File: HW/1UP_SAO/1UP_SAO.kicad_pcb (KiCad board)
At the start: 2 copper layers, 48 x 48 mm, 17 parts, among them X1 Badgelife_sao_connector_v169b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

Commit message: done?
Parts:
- moved R1 0.10 mm to (85.9, 101.5)
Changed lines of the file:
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@@
   )
   (module Resistor_SMD:R_0805_2012Metric_Pad1.15x1.40mm_HandSolder (layer B.Cu)
-    (at 85.8 101.5 180)
+    (at 85.9 101.5 180)
     (descr "Resistor SMD 0805 (2012 Metric), square (rectangular) end terminal, IPC_7351 nominal with elongated pad for handsoldering. (Body size source: https://docs.google.com/spreadsheets/d/1BsfQQcO9C6DZCsRaXUlFlo91Tg2WpOkGARC1WS5S8t0/edit?usp=sharing), generated with kicad-footprint-generator")
     (tags "resistor handsolder")
@@
   (segment (start 111.19559 102.27941) (end 111.975 101.5) (width 0.254) (layer B.Cu) (net 8))
   (segment (start 107.47059 102.27941) (end 111.19559 102.27941) (width 0.254) (layer B.Cu) (net 8))
-  (segment (start 92.75 102.5) (end 91.125 102.5) (width 0.254) (layer B.Cu) (net 8))
-  (segment (start 93.25 103) (end 92.75 102.5) (width 0.254) (layer B.Cu) (net 8))
+  (segment (start 111.975 101.5) (end 113.075 101.5) (width 0.254) (layer B.Cu) (net 8))
+  (segment (start 92.6 102.6) (end 91.225 102.6) (width 0.254) (layer B.Cu) (net 8))
+  (segment (start 93.25 103.25) (end 92.6 102.6) (width 0.254) (layer B.Cu) (net 8))
   (segment (start 97.52 107.75) (end 96.656401 106.886401) (width 0.254) (layer B.Cu) (net 8))
+  (segment (start 90.225 101.6) (end 87.2 101.6) (width 0.254) (layer B.Cu) (net 8))
   (segment (start 96.656401 106.886401) (end 94.136401 106.886401) (width 0.254) (layer B.Cu) (net 8))
-  (segment (start 91.125 102.5) (end 90.225 101.6) (width 0.254) (layer B.Cu) (net 8))
+  (segment (start 91.225 102.6) (end 90.225 101.6) (width 0.254) (layer B.Cu) (net 8))
   (segment (start 94.136401 106.886401) (end 93.25 106) (width 0.254) (layer B.Cu) (net 8))
-  (segment (start 90.225 101.6) (end 87.2 101.6) (width 0.254) (layer B.Cu) (net 8))
-  (segment (start 93.25 106) (end 93.25 103) (width 0.254) (layer B.Cu) (net 8))
-  (segment (start 111.975 101.5) (end 113.075 101.5) (width 0.254) (layer B.Cu) (net 8))
+  (segment (start 93.25 106) (end 93.25 103.25) (width 0.254) (layer B.Cu) (net 8))
   (zone (net 2) (net_name GND) (layer B.Cu) (hatch edge 0.508)
     (connect_pads (clearance 0))

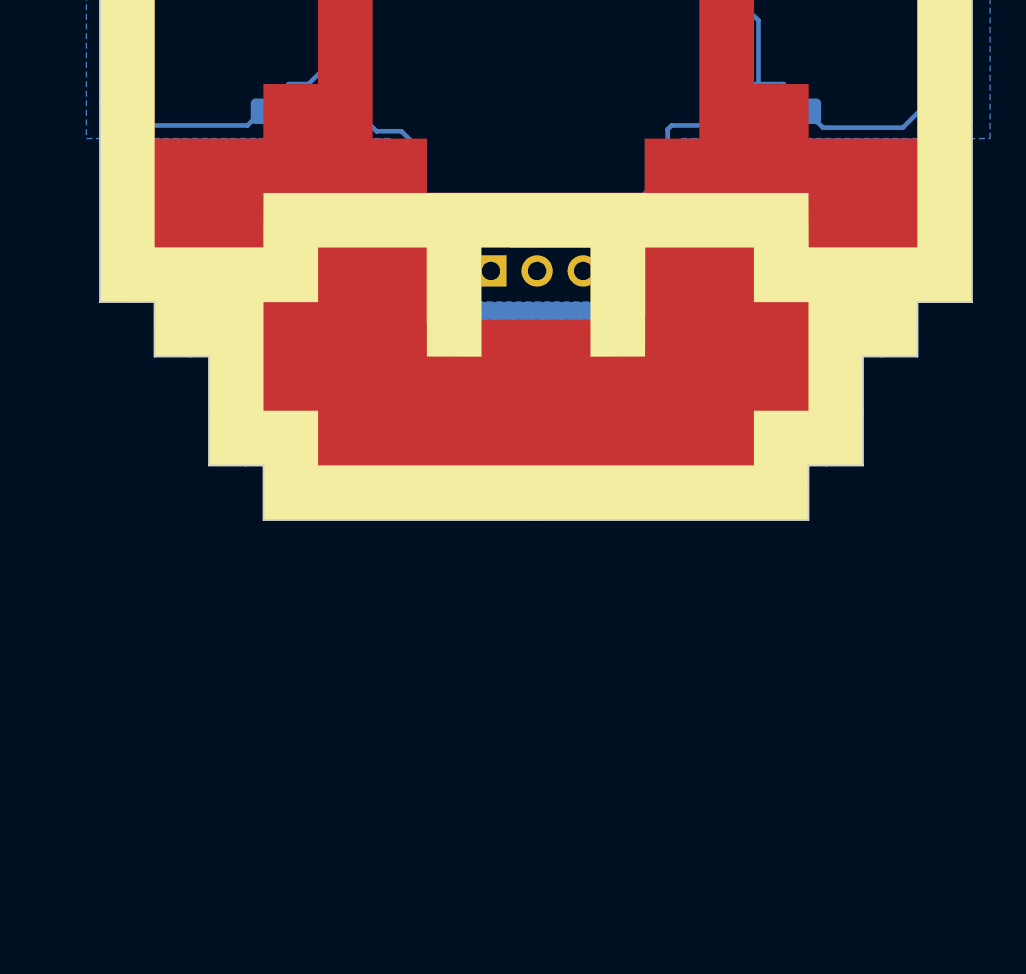
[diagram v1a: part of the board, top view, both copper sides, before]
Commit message: Removed D8 and D3, updated netlist and layout. moved circle on SAO header footprint
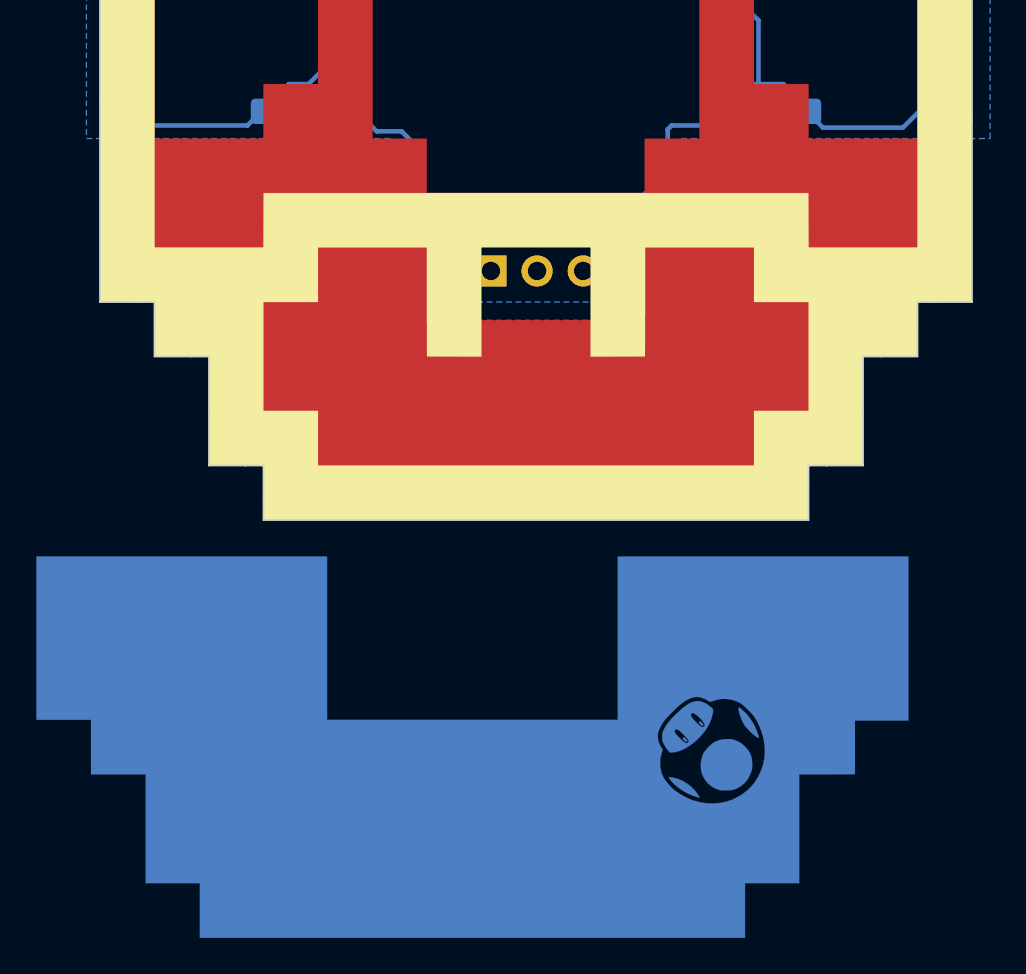
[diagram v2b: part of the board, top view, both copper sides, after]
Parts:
- removed the G*** at (100.0, 100.0)
- added G***: B.Silk, 1UP_SAO:B.Silk_g4152, F.Cu at (100.0, 100.0)
- G***: footprint LOGO -> 1UP_SAO:B.Cu_g4148
- moved G*** 23.3 mm to (96.5, 123.0)
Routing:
- net VCC: track 34.9 -> 34.0 mm

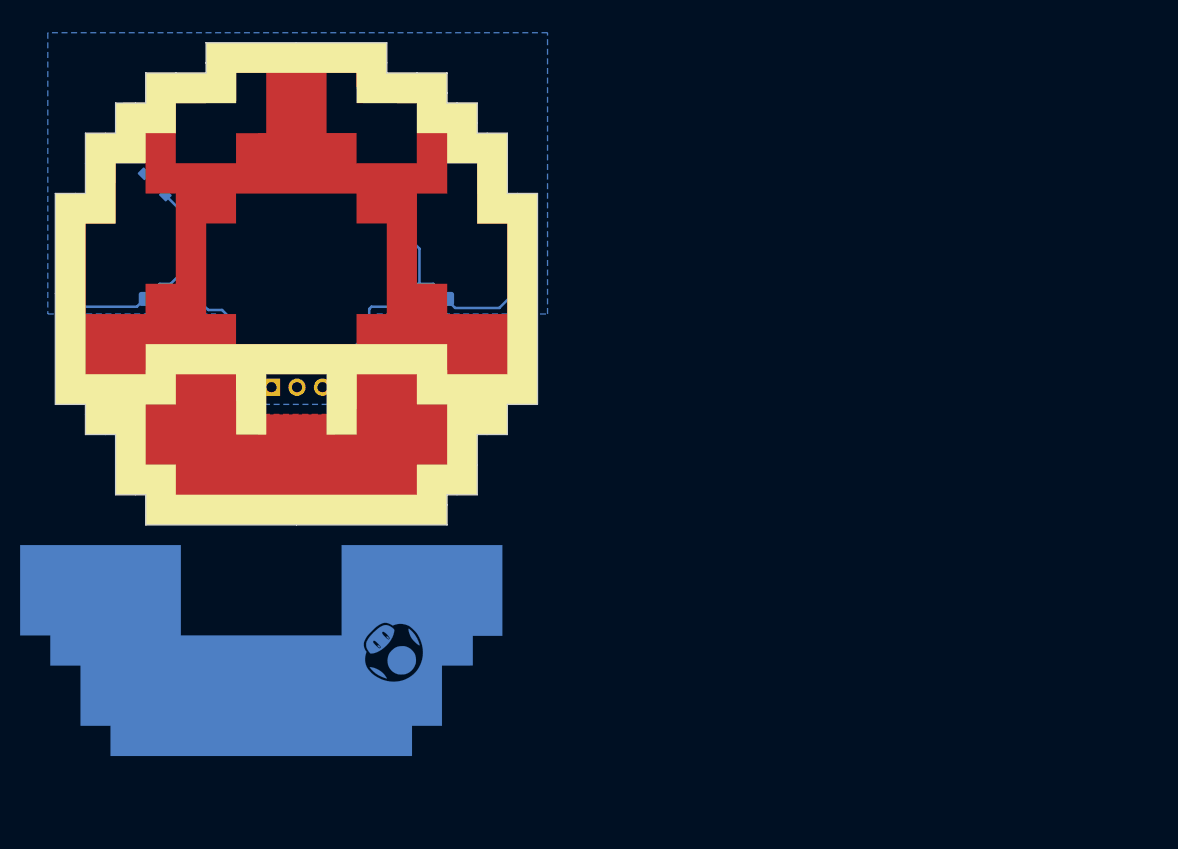
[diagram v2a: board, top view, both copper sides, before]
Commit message: Added B.cu and re-filled copper pour
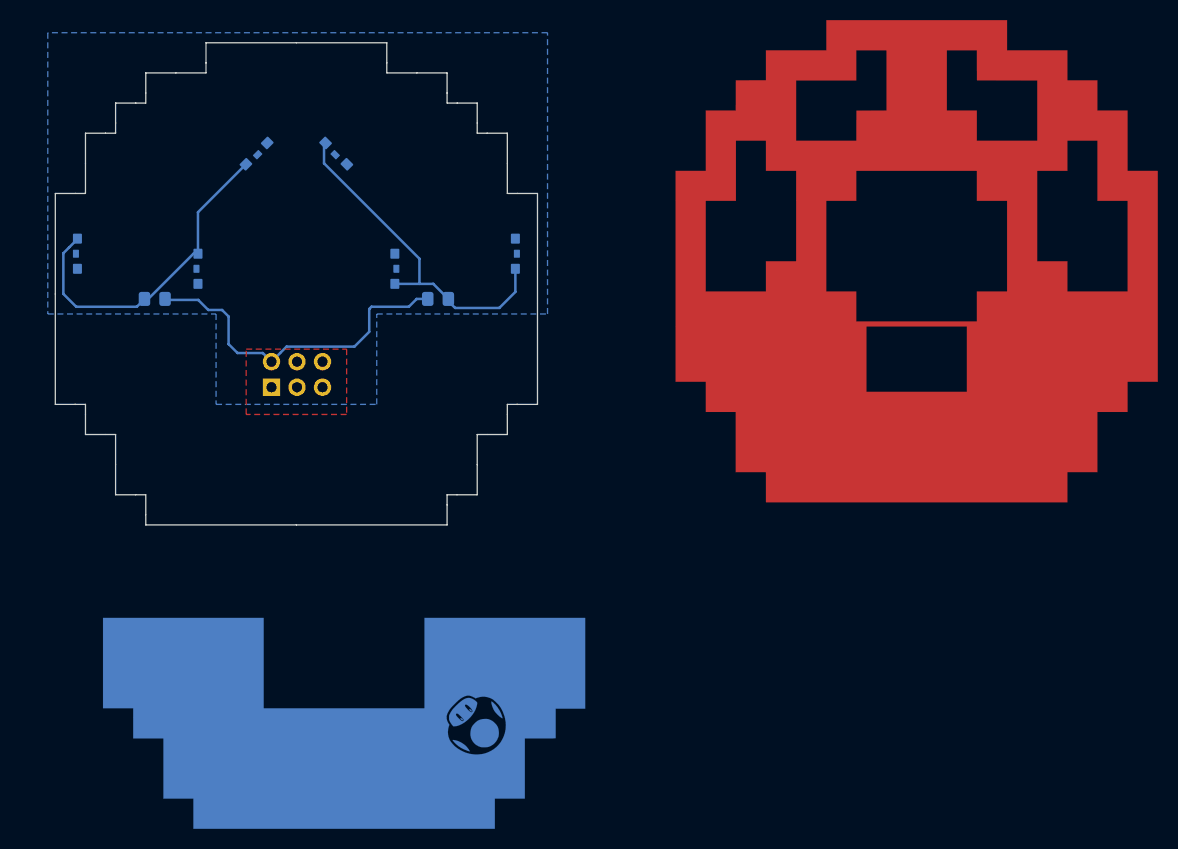
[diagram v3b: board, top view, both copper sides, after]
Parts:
- removed D3, D8: LED, 1UP_SAO:1204_SIDE_VIEW_LED
- removed the G*** at (100.0, 100.0)
- G***: value B.Cu -> LOGO
- moved G*** 61.8 mm to (161.8, 97.8)
- moved G*** 11.0 mm to (104.8, 130.2)
- moved D1 7.50 mm to (96.0, 87.0), turned to 225 degrees
- moved D4 1.50 mm to (78.2, 97.0)
- moved D5 0.25 mm to (104.0, 87.0)
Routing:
- net Net-(D1-Pad2): track 45.0 -> 33.1 mm
- net Net-(D5-Pad2): track 37.9 -> 34.1 mm

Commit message: Added #badgelife to B.Silk
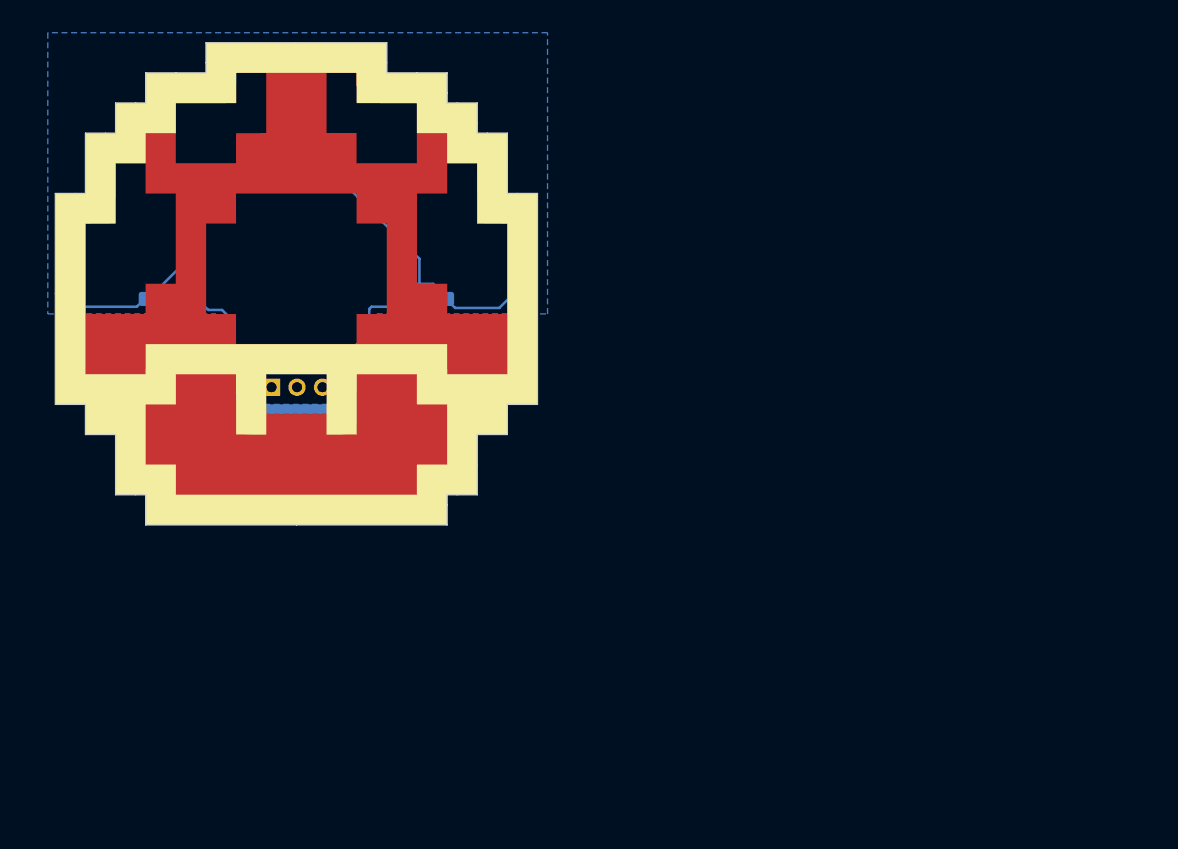
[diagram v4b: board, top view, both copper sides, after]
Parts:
- added G***: LOGO, 1UP_SAO:F.Silk_g4158, F.Cu at (100.0, 100.0)
- moved G*** 61.8 mm to (100.0, 100.0)
- moved G*** 30.6 mm to (100.0, 100.0)
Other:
- board text added: "@PCBWayOfficial"
